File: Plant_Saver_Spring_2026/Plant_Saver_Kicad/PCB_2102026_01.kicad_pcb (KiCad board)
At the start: 2 copper layers, 110 parts, among them J10 DM3D-SF, J11 Test, J2 SBH11-PBPC-D05-ST-BK, J3 SM04B-SRSS-TB, J5 Conn_01x02_Pin, J6 Conn_01x06_Socket, J7 S3B-PH-K-S, J8 54-00284, J9 1.25mm, Q1 G09P02L, Q10 G09P02L, Q11 ISP12DP06NMXTSA1, Q12 G09P02L, Q2 G09P02L, Q3 ISP12DP06NMXTSA1, Q4 G09P02L, Q5 G09P02L, Q6 G09P02L, Q7 G09P02L, Q8 G09P02L, Q9 G09P02L, SW1 Reset, SW2 25336NA, SW3 Boot, SW4 SA72SB0, U1 CDBA140SL-HF, U10 DW03C, U11 CDBA140SL-HF, U12 LP38511TJ-ADJ/NOPB, U13 MCP73833-xxx-UN, U14 MCP6234, U15 MCP73833-xxx-UN, U16 MCP6547T_I_MS, U2 CDBA140SL-HF, U3 CDBA140SL-HF, U4 CDBA140SL-HF, U5 ESP32-WROOM-32E-N16, U9 CDBA140SL-HF

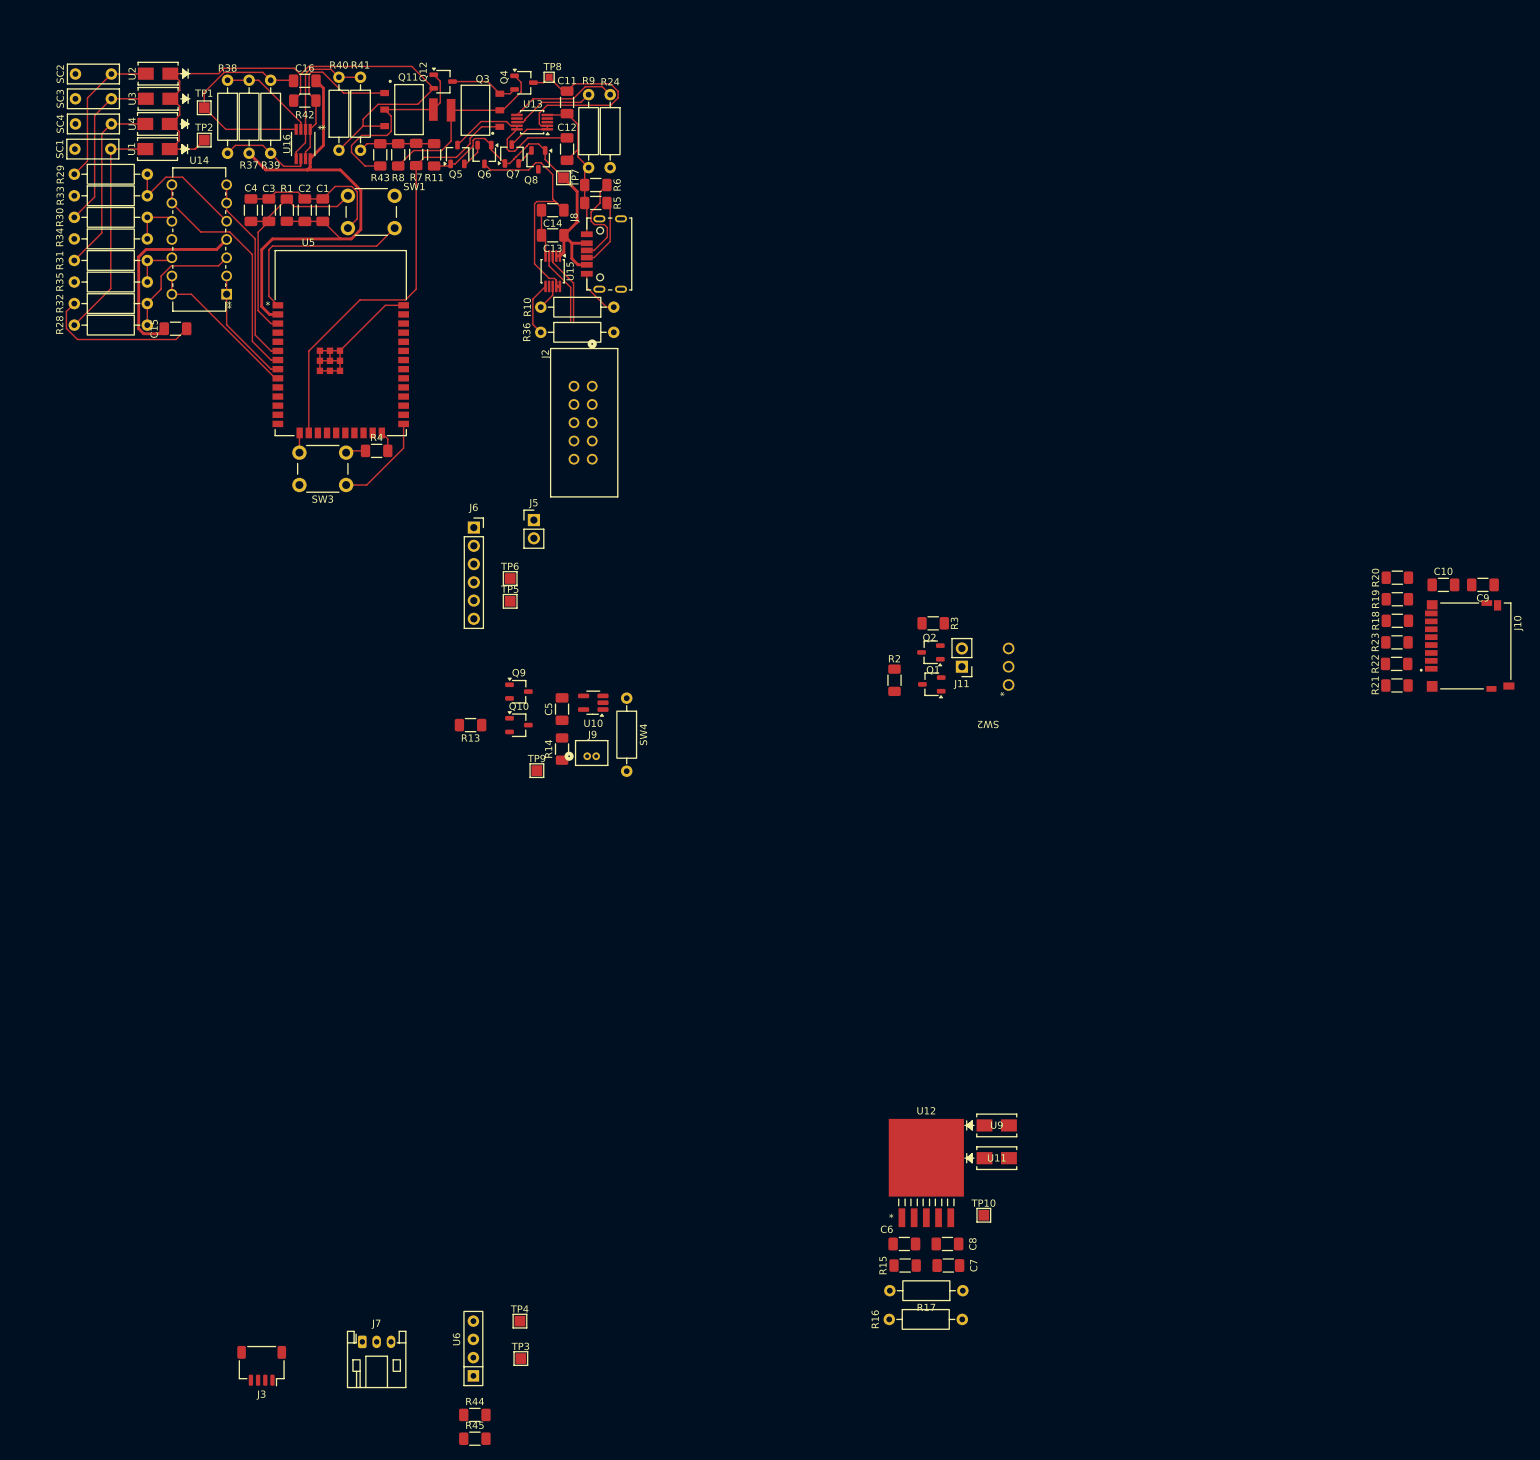
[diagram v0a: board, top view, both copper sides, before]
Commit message: PCB Routing
I believe this to be the product of mania, but it may yet function.
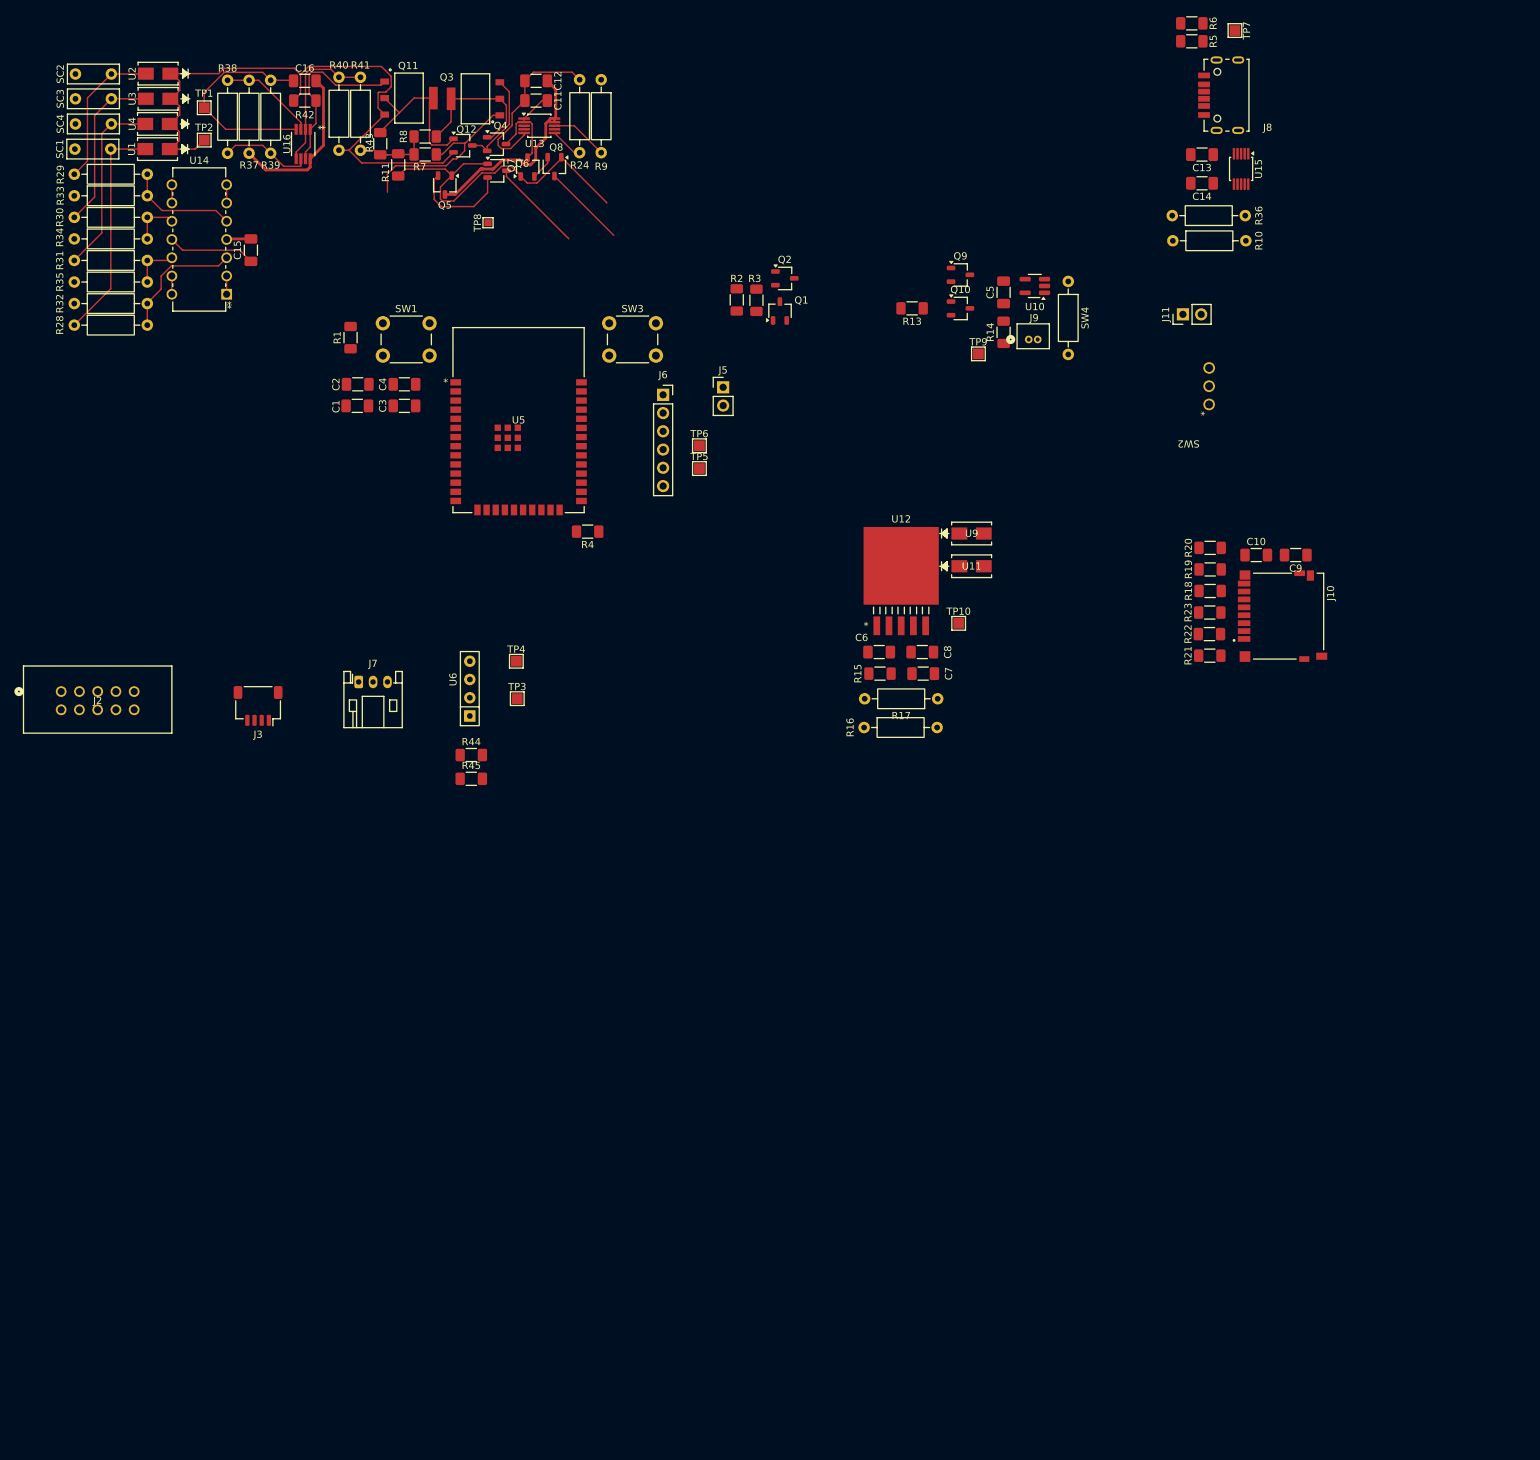
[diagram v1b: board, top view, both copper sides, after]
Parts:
- moved R36 99.4 mm to (192.9, 90.8), turned to 180 degrees
- moved U15 96.9 mm to (192.3, 84.3)
- moved TP7 95.7 mm to (191.4, 65.0)
- moved TP4 91.8 mm to (91.4, 152.8)
- moved J3 91.8 mm to (55.5, 159.0)
- moved J7 91.8 mm to (69.5, 155.7)
- moved R44 91.8 mm to (85.2, 165.8)
- moved R45 91.8 mm to (85.2, 169.1)
- moved TP3 91.8 mm to (91.6, 158.0)
- moved U6 91.8 mm to (85.0, 160.4)
- moved C13 91.1 mm to (186.9, 82.3)
- moved C14 90.4 mm to (186.9, 86.3)
- moved J8 88.7 mm to (189.0, 74.0)
- moved R5 85.9 mm to (185.4, 66.5)
- moved R6 85.9 mm to (185.4, 64.0)
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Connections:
- U5 pad 6: V_Solar2 -> V_Solar1
- U5 pad 7: V_Solar3 -> V_Solar2
- U5 pad 8: V_Solar1 -> V_Solar3
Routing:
- net GND: track 181.2 -> 76.9 mm
- net Vbus: track 71.0 -> 22.8 mm
- net Solar_Chg_EN: track 61.4 -> 26.8 mm
- net Net-(U5-EN): track 32.7 -> 0.00 mm
- net V_Solar3: track 33.4 -> 2.54 mm
- net V_Solar2: track 26.6 -> 2.54 mm
- net Vperiph: track 27.5 -> 3.92 mm
- net /Power_And_Charging/MCP73833_USB/Vbat: track 35.3 -> 13.1 mm
- net /Power_And_Charging/MCP73833_Solar/Vin: track 35.6 -> 15.5 mm
- net V_Solar4: track 22.1 -> 2.54 mm
- net V_Solar1: track 16.5 -> 2.54 mm
- net Net-(J8-CC2): track 13.5 -> 0.00 mm
- net Net-(U5-IO0): track 13.5 -> 0.00 mm
- net Net-(Q10-G): track 0.00 -> 11.7 mm
- net Net-(Q5-S): track 3.53 -> 14.3 mm
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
